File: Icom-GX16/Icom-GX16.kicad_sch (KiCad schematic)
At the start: 6 parts, among them J1 Mic Input, J2 Base Board, J3 Headphone/Speaker Input

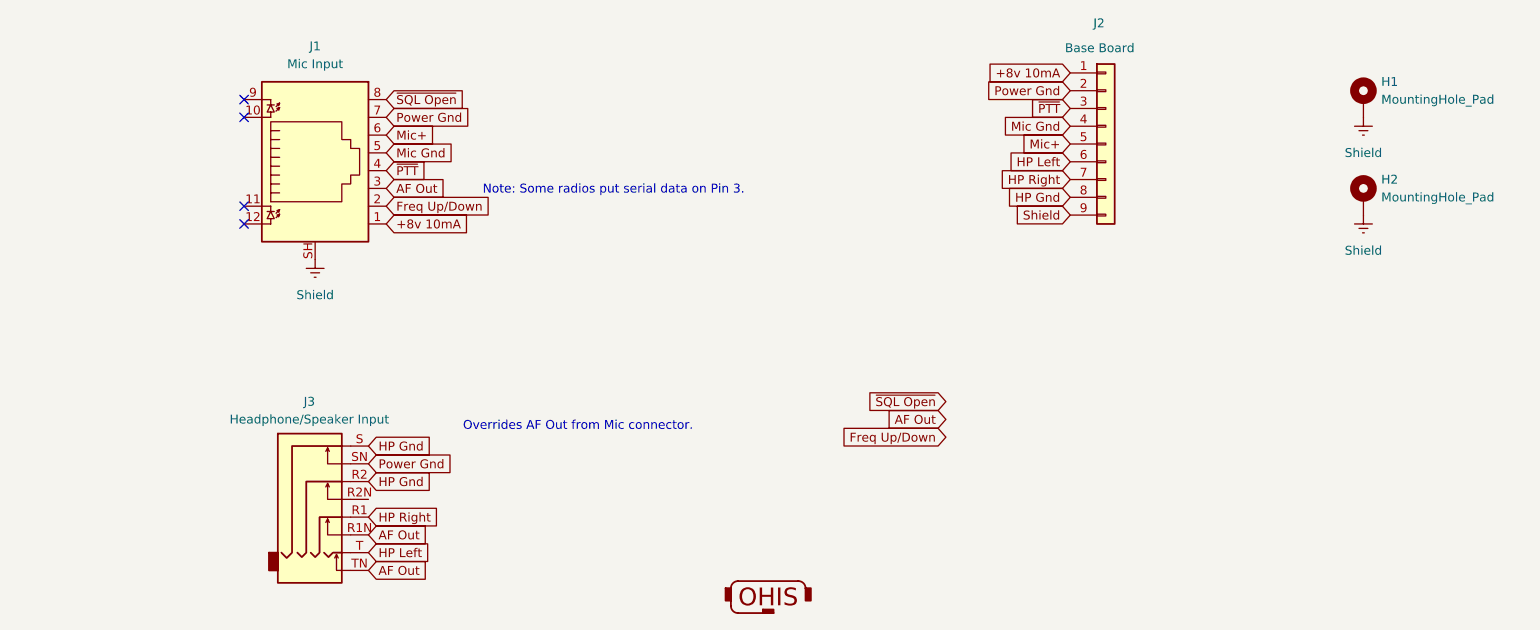
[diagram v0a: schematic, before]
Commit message: Icom-GX16 added. Also GX16 riser board. #1
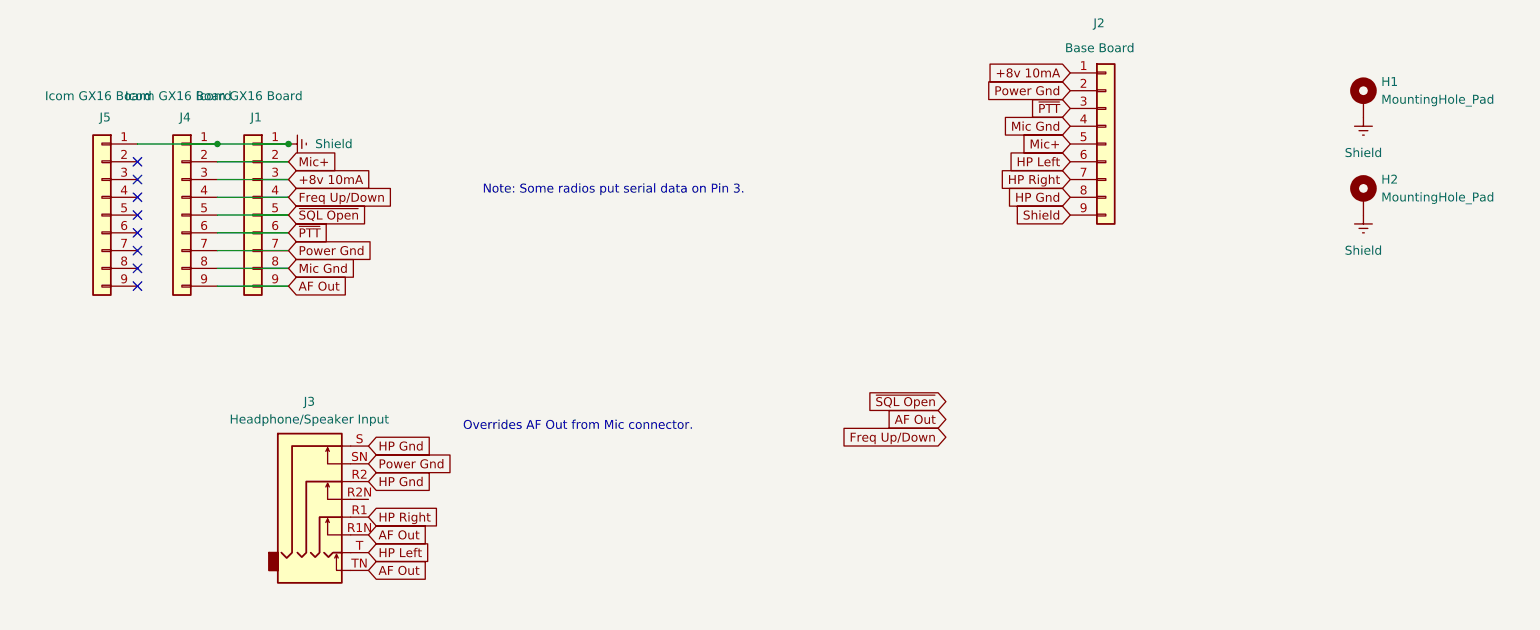
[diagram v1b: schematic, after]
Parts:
- removed G1: Logo_OHIS, OHIS:Logo_OHIS_Medium, symbol OHIS:Logo_OHIS
- removed J1: Mic Input, Connector_RJ:RJ45_Amphenol_RJHSE538X, symbol Connector:RJ45_LED_Shielded
- added J1: Icom GX16 Board, Libraries:Conn_B2B-RA_2.54mm_9pin_RtoL, symbol Connector_Generic:Conn_01x09
- added J4, J5: Icom GX16 Board, Libraries:Conn_B2B-RA_2.54mm_9pin_LtoR, symbol Connector_Generic:Conn_01x09
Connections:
- net +8v 10mA: now also J1.3 (Pin_3), J4.3 (Pin_3)
- net AF Out: now also J1.9 (Pin_9), J4.9 (Pin_9)
- net Freq Up/Down: now also J1.4 (Pin_4), J4.4 (Pin_4)
- net Mic Gnd: now also J1.8 (Pin_8), J4.8 (Pin_8)
- net Mic+: now also J1.2 (Pin_2), J4.2 (Pin_2)
- net Power Gnd: now also J1.7 (Pin_7), J4.7 (Pin_7)
- net Shield: now also J1.1 (Pin_1), J4.1 (Pin_1), J5.1 (Pin_1)
- net ~{PTT}: now also J1.6 (Pin_6), J4.6 (Pin_6)
- net ~{SQL Open}: now also J1.5 (Pin_5), J4.5 (Pin_5)
- no-connect marks 4 -> 8
